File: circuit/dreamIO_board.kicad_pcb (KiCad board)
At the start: 2 copper layers, 60 x 60 mm, 82 parts, among them IC1 TPS61200, P1 BATT, P2 CONN_01X08, P3 CONN_01X08, P4 CONN_01X02, P5 CONN_01X06, P6 gnd_con, P7 CONN_01X03, P8 NO_CASCADE, P9 PixelOut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

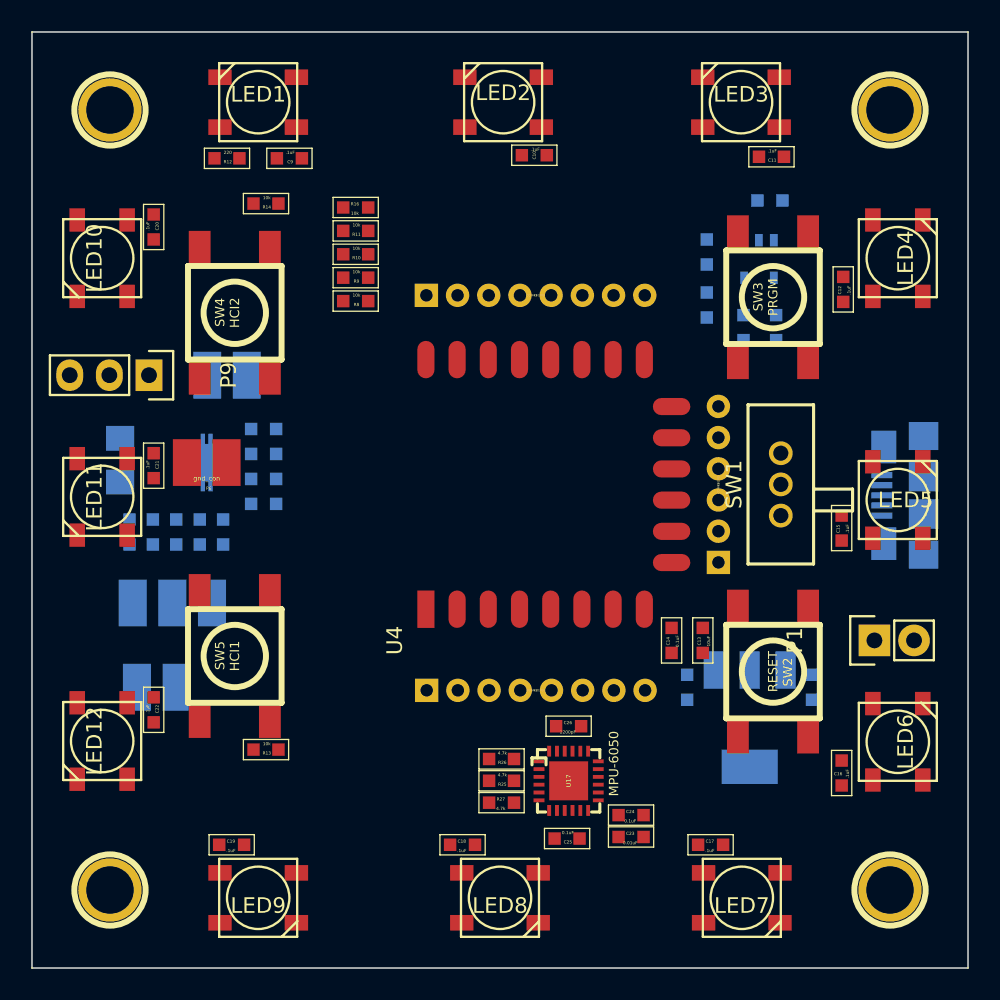
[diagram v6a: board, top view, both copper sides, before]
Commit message: changed pinout for MPU6050 to include groundplane under area. started on routing
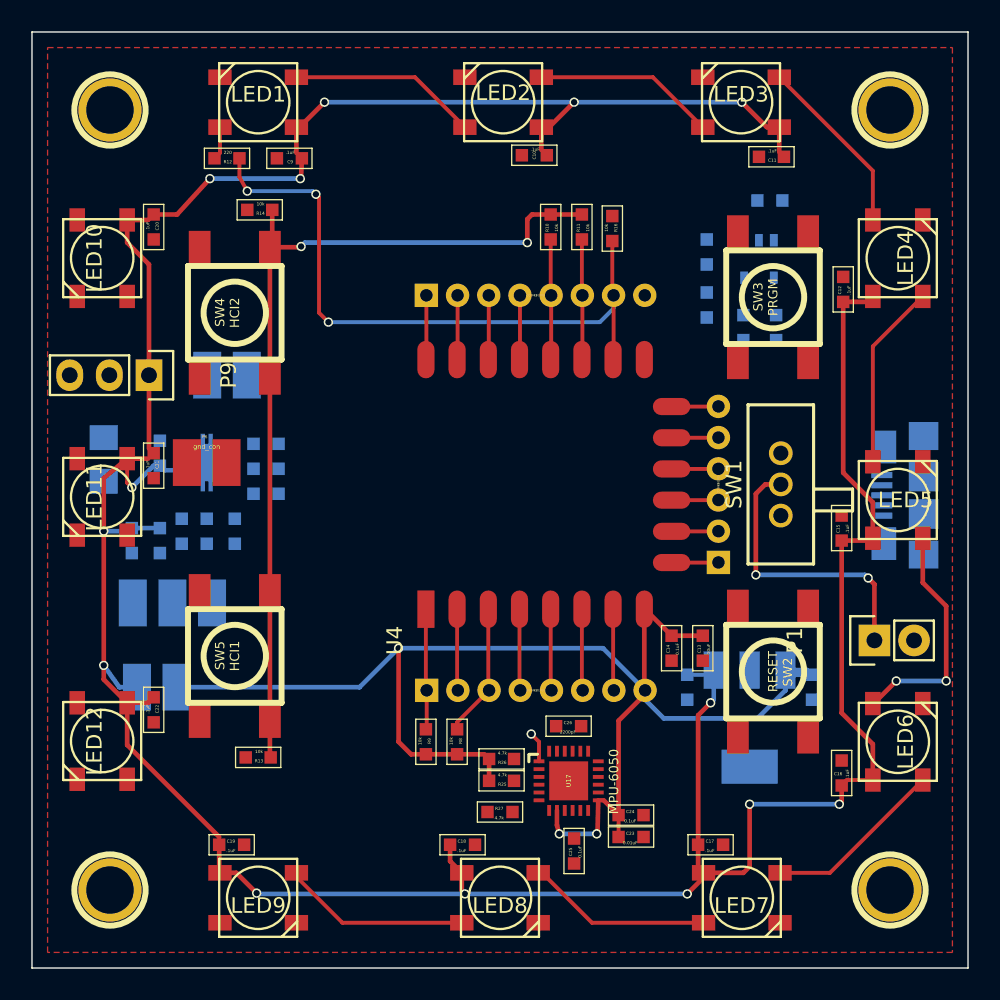
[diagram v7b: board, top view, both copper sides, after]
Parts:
- U17: footprint kicad-libraries:QFN-24-4x4-EP -> mpu6050:QFN-24-4x4-EP_steevedit
- moved R9 30.1 mm to (39.5, 59.2), turned to 90 degrees
- moved R8 29.0 mm to (41.5, 59.2), turned to 90 degrees
- moved R16 16.5 mm to (51.5, 26.3), turned to 90 degrees
- moved R11 14.5 mm to (49.5, 26.2), turned to 270 degrees
- moved R10 12.6 mm to (47.5, 26.2), turned to 270 degrees
- moved R3 9.19 mm to (29.3, 40.1), turned to 180 degrees
- moved C6 8.39 mm to (23.9, 45.7), turned to 270 degrees
- moved C5 6.65 mm to (22.5, 40.7), turned to 90 degrees
- moved R4 1.19 mm to (22.5, 46.3)
- moved L1 1.05 mm to (18.9, 41.1)
- moved C25 0.92 mm to (49.0, 66.2), turned to 270 degrees
- moved R7 0.75 mm to (27.3, 45.7)
- moved R13 0.71 mm to (28.8, 60.2)
- moved C4 0.67 mm to (30.1, 42.5)
- moved C3 0.67 mm to (28.5, 42.5)
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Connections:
- U17 pad 25: (no net) -> GND
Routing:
- net VCC: track 0.00 -> 220.8 mm, vias 0 -> 14
- net +3V3: track 0.00 -> 146.2 mm, vias 0 -> 5
- net GPIO15: track 0.00 -> 42.4 mm, vias 0 -> 3
- net +BATT: track 0.00 -> 18.5 mm, vias 0 -> 2
- net Net-(LED5-Pad2): track 0.00 -> 15.1 mm, vias 0 -> 2
- net Net-(LED1-Pad2): track 0.00 -> 12.1 mm
- net Net-(LED8-Pad2): track 0.00 -> 12.1 mm
- net Net-(LED7-Pad2): track 0.00 -> 11.9 mm
- net Net-(LED4-Pad2): track 0.00 -> 11.9 mm
- net Net-(LED2-Pad2): track 0.00 -> 11.7 mm
- net Net-(LED3-Pad2): track 0.00 -> 11.6 mm
- net Net-(LED6-Pad2): track 0.00 -> 11.6 mm
- net CH_PD: track 0.00 -> 8.57 mm
- net RESET: track 0.00 -> 7.74 mm
- net GPIO2: track 0.00 -> 7.72 mm
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- added copper zone on F.Cu, net GND

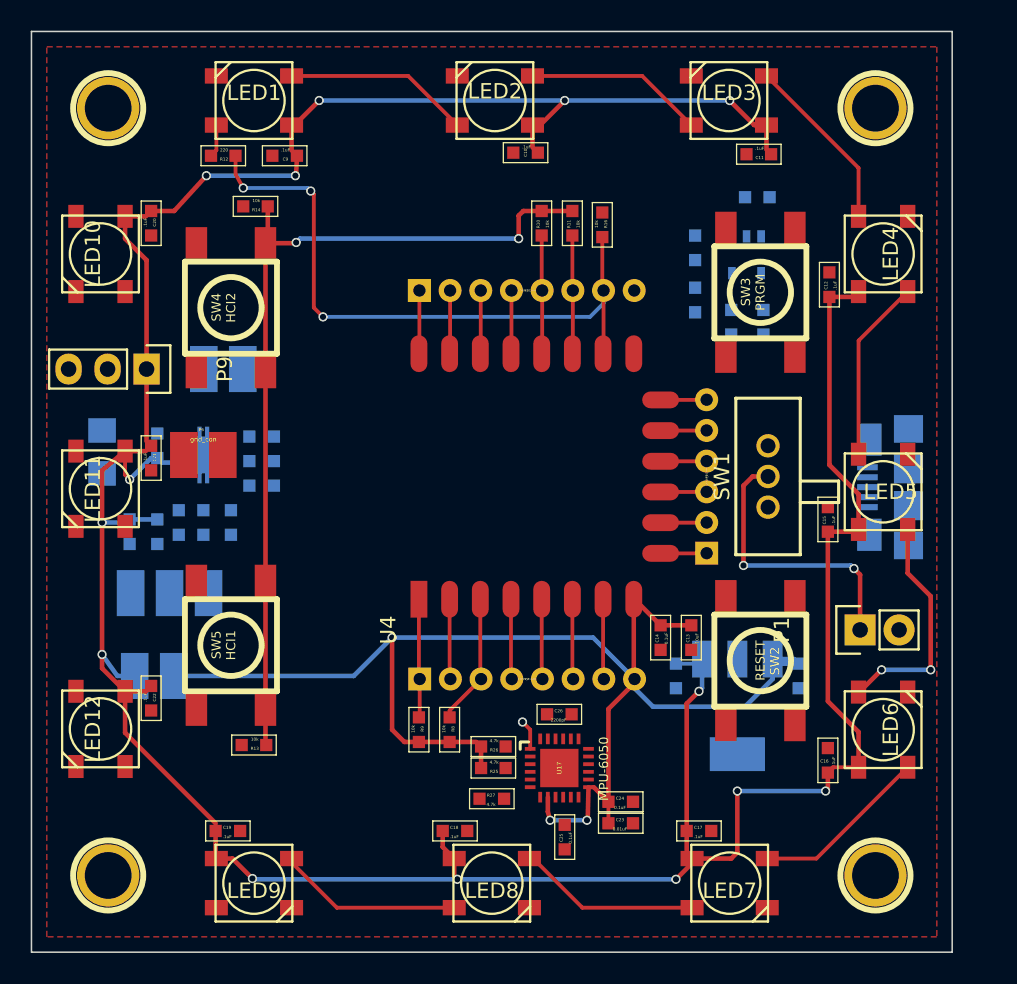
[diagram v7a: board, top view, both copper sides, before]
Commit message: routed some traces. May need to go back in and clean some up.
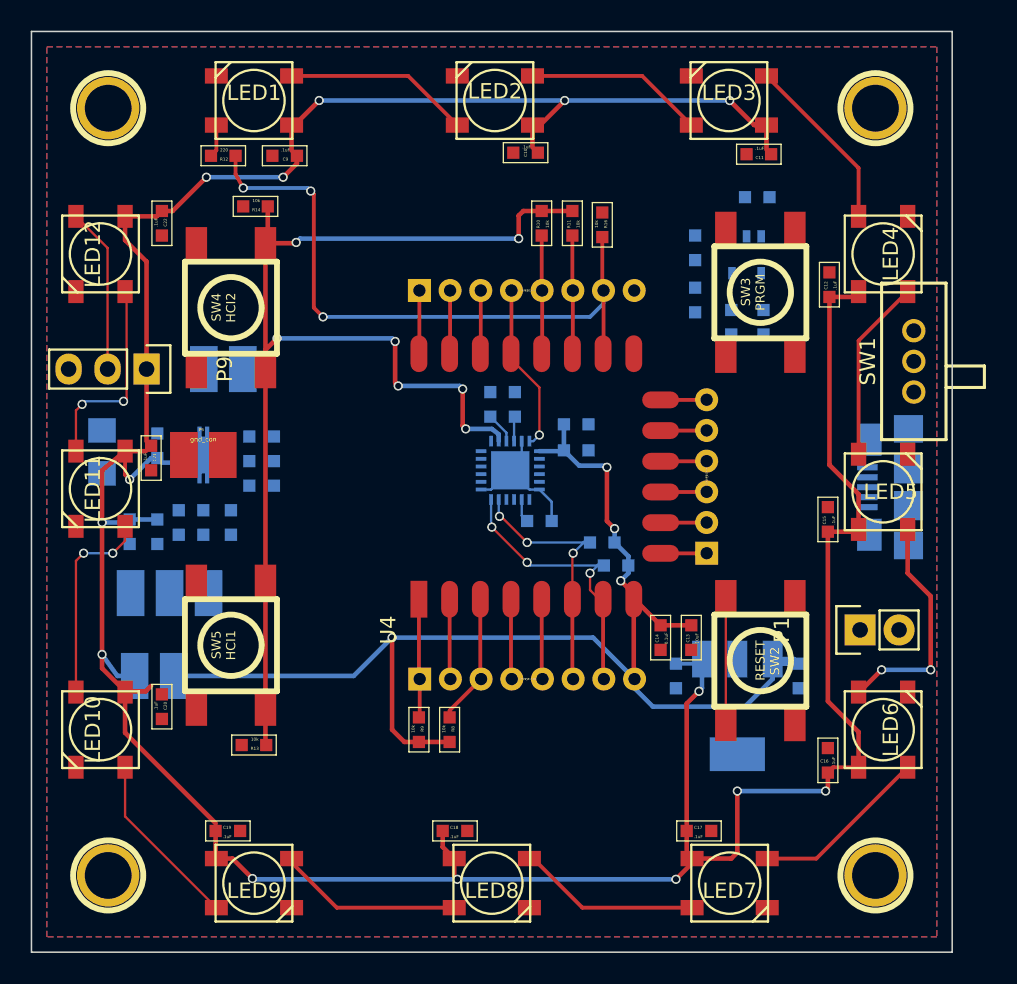
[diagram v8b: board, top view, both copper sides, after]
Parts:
- C23, C24, C25, C26, R25, R26, R27, U17: moved to B.Cu
- moved C20 31.5 mm to (22.8, 57.7)
- moved LED10 31.0 mm to (18.8, 59.2)
- moved C22 31.0 mm to (22.8, 26.2)
- moved LED12 30.9 mm to (18.8, 28.2)
- moved C25 28.4 mm to (45.8, 38.0), turned to 90 degrees
- moved R27 25.7 mm to (44.2, 38.0), turned to 90 degrees
- moved C24 24.8 mm to (49.8, 39.3)
- moved C23 24.5 mm to (49.8, 41.0)
- moved U17 19.7 mm to (45.5, 42.3), turned to 90 degrees
- moved R25 16.3 mm to (51.5, 47.0), turned to 180 degrees
- moved R26 14.3 mm to (52.4, 48.5), turned to 180 degrees
- moved C26 12.7 mm to (47.4, 45.6), turned to 0 degrees
- moved SW1 12.1 mm to (71.8, 35.2)
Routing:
- net +BATT: track 18.5 -> 0.00 mm, vias 2 -> 0
- net +3V3: track 146.2 -> 164.3 mm, vias 5 -> 11
- net GPIO13: track 5.22 -> 18.7 mm, vias 0 -> 3
- net Net-(LED11-Pad2): track 0.00 -> 13.3 mm, vias 0 -> 2
- net Net-(LED10-Pad2): track 0.00 -> 13.2 mm, vias 0 -> 2
- net GPIO12: track 5.22 -> 17.4 mm, vias 0 -> 3
- net Net-(LED10-Pad4): track 0.00 -> 11.6 mm
- net DOUT: track 0.00 -> 10.8 mm
- net RESET: track 7.74 -> 16.1 mm
- net GND: track 1.96 -> 9.43 mm, vias 1 -> 0
- net GPIO4: track 4.13 -> 11.0 mm, vias 0 -> 1
- net ADO: track 0.00 -> 2.04 mm
- net Net-(C25-Pad1): track 0.00 -> 1.62 mm
- net Net-(C26-Pad1): track 0.00 -> 1.55 mm
- added copper zone on B.Cu, net GND
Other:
- net class Default: clearance 0.2 -> 0.1524; trace_width 0.25 -> 0.1524
- rule trace_clearance: 0.2 -> 0.1524
- rule trace_min: 0.2 -> 0.1524
